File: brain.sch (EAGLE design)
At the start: 28 parts, among them IC1 LP2950ACZ-3.3, IC2 LP2950ACZ-3.3, U1 TINY45-20-DIP, U4 TINY45-20-DIP, U5 TINY45-20-DIP, U6 TINY45-20-DIP

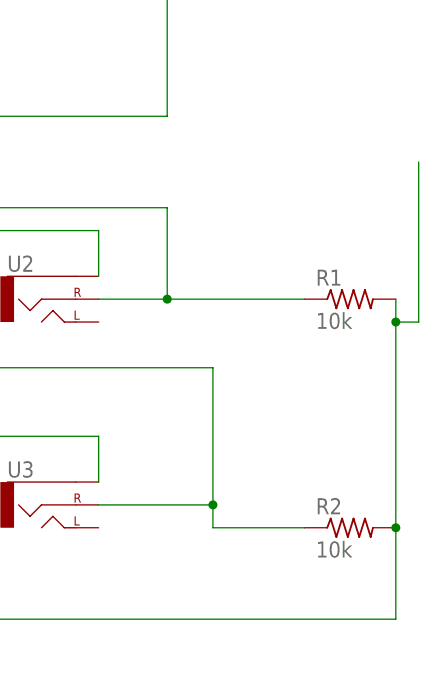
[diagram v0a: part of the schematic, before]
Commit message: Redid a lot of the routing for wire width and such. pre-changing a few back to smaller wires.
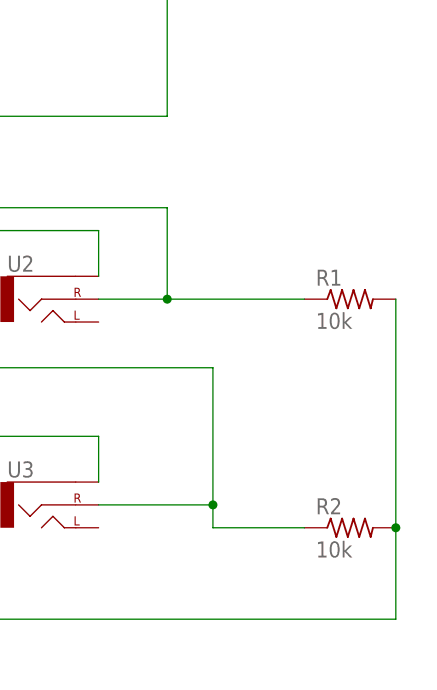
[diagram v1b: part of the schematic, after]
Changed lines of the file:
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@@
 <pinref part="R2" gate="G$1" pin="2"/>
 <pinref part="R1" gate="G$1" pin="2"/>
-<wire x1="167.64" y1="-10.16" x2="167.64" y2="-12.7" width="0.1524" layer="91"/>
-<wire x1="170.18" y1="5.08" x2="170.18" y2="-12.7" width="0.1524" layer="91"/>
-<wire x1="170.18" y1="-12.7" x2="167.64" y2="-12.7" width="0.1524" layer="91"/>
-<junction x="167.64" y="-12.7"/>
-<wire x1="167.64" y1="-12.7" x2="167.64" y2="-35.56" width="0.1524" layer="91"/>
+<wire x1="167.64" y1="-10.16" x2="167.64" y2="-35.56" width="0.1524" layer="91"/>
 <junction x="167.64" y="-35.56"/>
 <wire x1="167.64" y1="-35.56" x2="167.64" y2="-45.72" width="0.1524" layer="91"/>
